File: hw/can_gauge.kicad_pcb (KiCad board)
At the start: 2 copper layers, 31 parts, among them J1 Gauge 1, J2 Gauge 2, J3 Gauge 3, J4 Gauge 4, J5 Gauge 5, J6 Gauge 6, J7 Power & CAN, J8 USB_B, U1 PIC16F1459-IP, U4 74HC595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

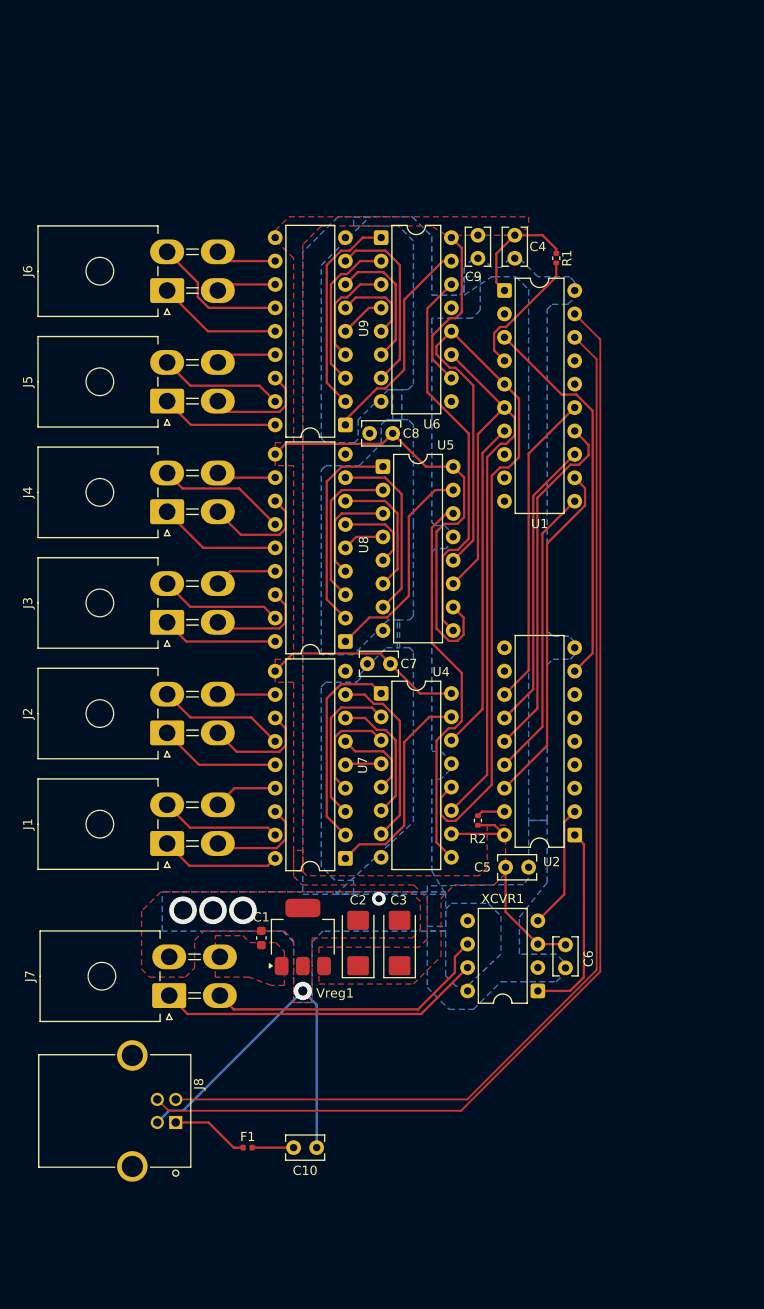
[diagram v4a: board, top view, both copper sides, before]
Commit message: hw: schematic page setup; fix usb wiring
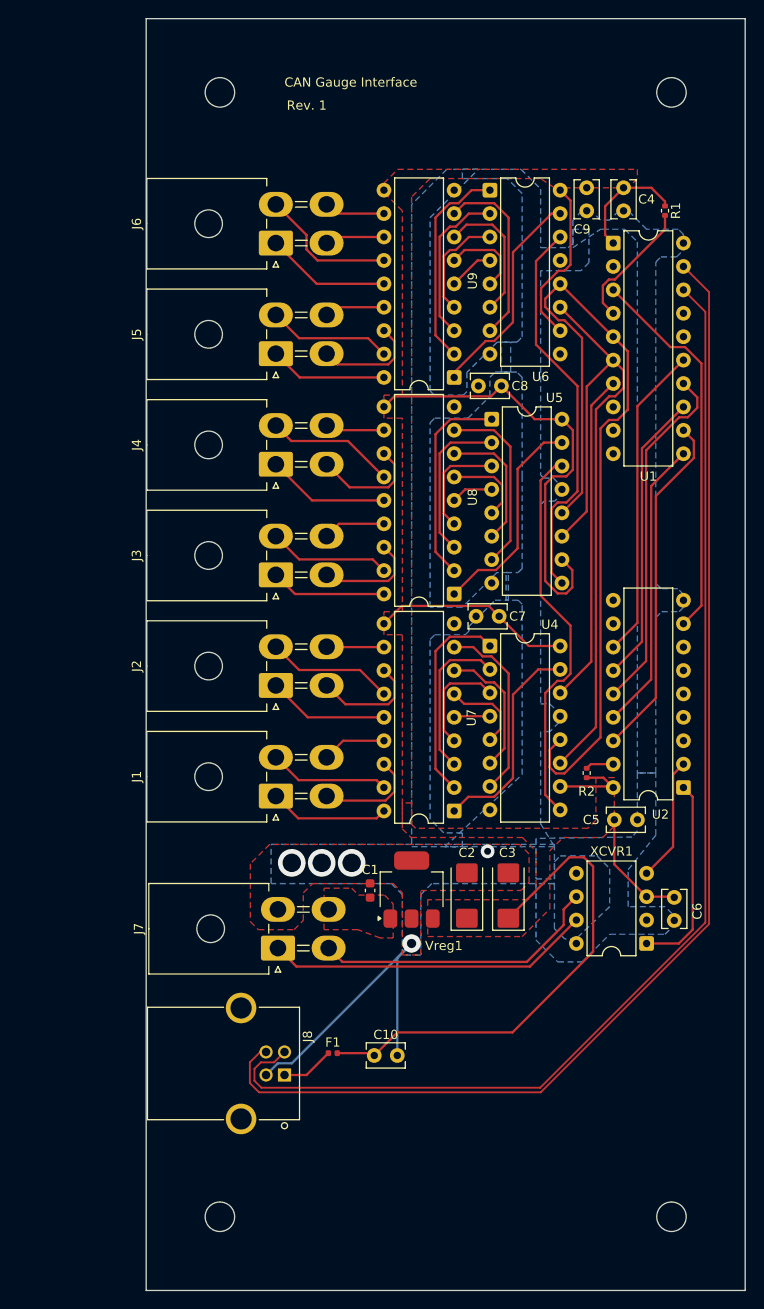
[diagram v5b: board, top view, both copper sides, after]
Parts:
- moved F1 13.8 mm to (70.2, 162.2)
- moved C10 13.3 mm to (77.2, 162.5)
- moved U1 12.9 mm to (100.7, 74.3)
- moved U5 12.9 mm to (87.5, 93.5)
- moved J1 12.9 mm to (64.1, 134.3)
- moved J2 12.9 mm to (64.1, 122.3)
- moved J3 12.9 mm to (64.1, 110.3)
- moved J4 12.9 mm to (64.1, 98.3)
- moved J5 12.9 mm to (64.1, 86.3)
- moved J6 12.9 mm to (64.1, 74.3)
- moved J8 12.9 mm to (65.0, 164.6)
- moved C1 12.9 mm to (74.3, 144.6)
- moved C2 12.9 mm to (84.8, 145.2)
- moved C3 12.9 mm to (89.3, 145.2)
- moved C4 12.9 mm to (101.8, 68.3)
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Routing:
- net +5V: track 128.7 -> 178.4 mm
- net USB-: track 121.1 -> 131.6 mm
- net USB+: track 127.3 -> 134.8 mm
- net GND: track 39.3 -> 34.5 mm
- net Net-(J8-VBUS): track 8.45 -> 5.74 mm
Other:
- board outline added: 65 x 138 mm
- board text added: "CAN Gauge Interface"
- board text added: "Rev. 1"

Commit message: hw: shrink board
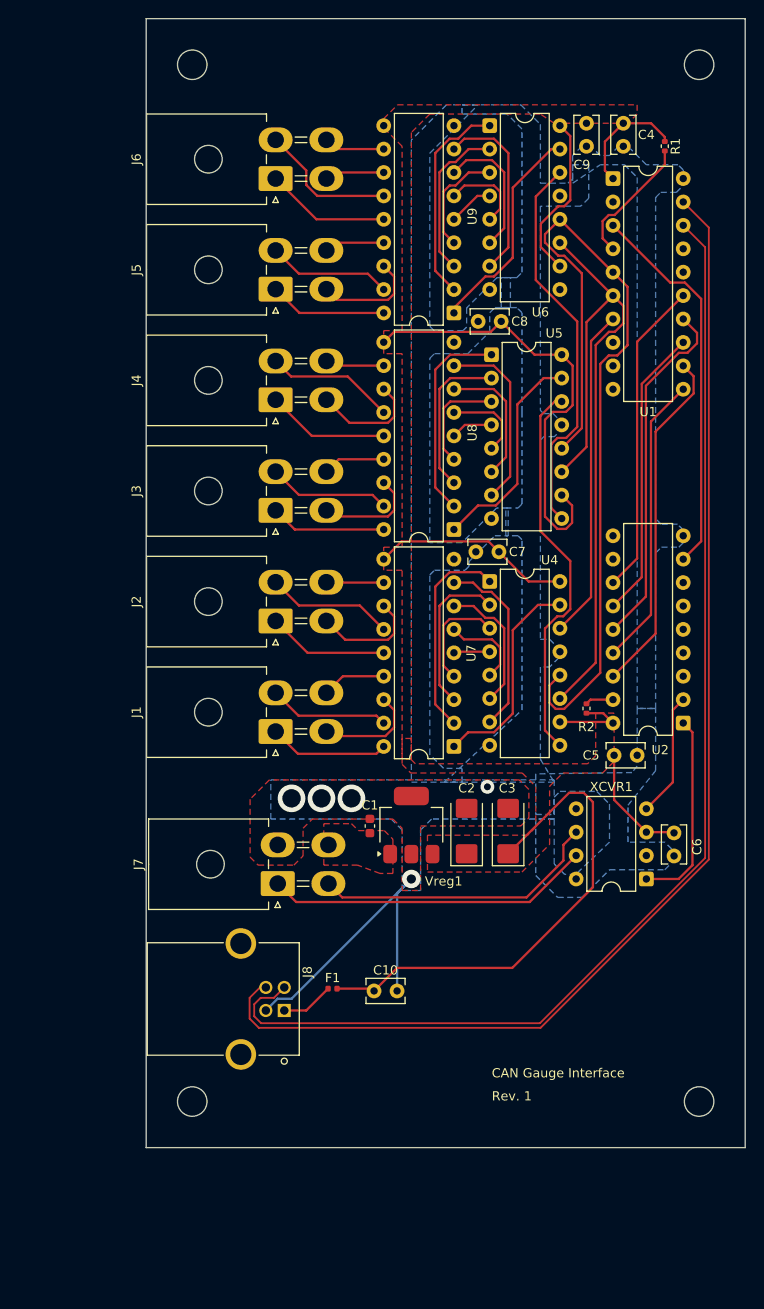
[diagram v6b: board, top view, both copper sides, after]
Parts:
- added REF**: MountingHole_3.2mm_M3, MountingHole:MountingHole_3.2mm_M3, F.Cu at (55.0, 55.0)
- added REF**: MountingHole_3.2mm_M3, MountingHole:MountingHole_3.2mm_M3, F.Cu at (55.0, 167.5)
- added REF**: MountingHole_3.2mm_M3, MountingHole:MountingHole_3.2mm_M3, F.Cu at (110.0, 167.5)
- added REF**: MountingHole_3.2mm_M3, MountingHole:MountingHole_3.2mm_M3, F.Cu at (110.0, 55.0)
- moved C1 7.00 mm to (74.3, 137.6)
- moved C10 7.00 mm to (77.2, 155.5)
- moved C2 7.00 mm to (84.8, 138.2)
- moved C3 7.00 mm to (89.3, 138.2)
- moved C5 7.00 mm to (100.8, 129.9)
- moved C6 7.00 mm to (107.3, 138.3)
- moved C7 7.00 mm to (88.3, 107.8)
- moved C8 7.00 mm to (88.5, 82.8)
- moved F1 7.00 mm to (70.2, 155.2)
- moved J1 7.00 mm to (64.0, 127.3)
- moved J2 7.00 mm to (64.0, 115.3)
- moved J3 7.00 mm to (64.0, 103.3)
- moved J4 7.00 mm to (64.0, 91.3)
- moved J5 7.00 mm to (64.0, 79.3)
- moved J6 7.00 mm to (64.0, 67.3)
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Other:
- board size 65 x 138 mm -> 65 x 122.5 mm

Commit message: hw: fix clipped silkscreen
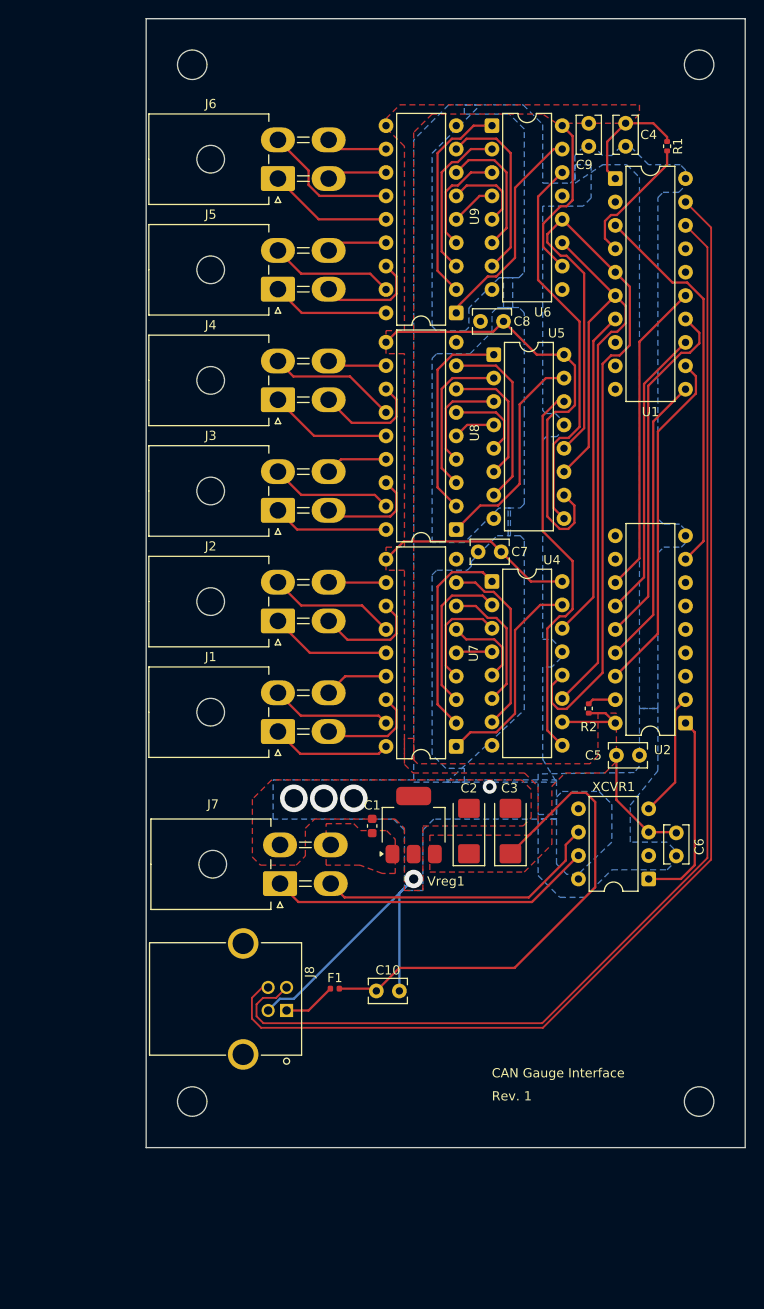
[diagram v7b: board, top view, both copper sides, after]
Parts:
- moved C1 0.25 mm to (74.5, 137.6)
- moved C10 0.25 mm to (77.5, 155.5)
- moved C2 0.25 mm to (85.0, 138.2)
- moved C3 0.25 mm to (89.5, 138.2)
- moved C4 0.25 mm to (102.0, 61.4)
- moved C5 0.25 mm to (101.0, 129.9)
- moved C6 0.25 mm to (107.5, 138.3)
- moved C7 0.25 mm to (88.5, 107.8)
- moved C8 0.25 mm to (88.8, 82.8)
- moved C9 0.25 mm to (98.0, 61.4)
- moved F1 0.25 mm to (70.5, 155.2)
- moved J1 0.25 mm to (64.3, 127.3)
- moved J2 0.25 mm to (64.3, 115.3)
- moved J3 0.25 mm to (64.3, 103.3)
- moved J4 0.25 mm to (64.3, 91.3)
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
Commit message: hw: generate bom and cpl
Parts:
- C1: value 0.47 uF -> 0.47u
- C10, C4, C5, C6, C7, C8, C9: value 0.1 uF -> 0.1u
- C2, C3: value 22 uF -> 22u
- F1: value 500 mA -> 500m
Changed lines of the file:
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@@
 			)
 		)
-		(property "Value" "0.1 uF"
+		(property "Value" "0.1u"
 			(at 1.25 2.5 90)
 			(layer "F.Fab")
@@
 			)
 		)
-		(property "Value" "500 mA"
+		(property "Value" "500m"
 			(at 0 1.17 0)
 			(layer "F.Fab")
@@
 			)
 		)
-		(property "Value" "0.1 uF"
+		(property "Value" "0.1u"
 			(at 1.25 2.5 0)
 			(layer "F.Fab")
@@
 			)
 		)
-		(property "Value" "0.47 uF"
+		(property "Value" "0.47u"
 			(at 0 1.43 90)
 			(layer "F.Fab")
@@
 			)
 		)
-		(property "Value" "0.1 uF"
+		(property "Value" "0.1u"
 			(at 1.25 2.5 0)
 			(layer "F.Fab")
@@
 			)
 		)
-		(property "Value" "0.1 uF"
+		(property "Value" "0.1u"
 			(at 1.25 2.5 0)
 			(layer "F.Fab")
@@
 			)
 		)
-		(property "Value" "22 uF"
+		(property "Value" "22u"
 			(at 0 2.55 90)
 			(layer "F.Fab")
@@
 			)
 		)
-		(property "Value" "0.1 uF"
+		(property "Value" "0.1u"
 			(at 1.25 2.5 90)
 			(layer "F.Fab")
@@
 			)
 		)
-		(property "Value" "22 uF"
+		(property "Value" "22u"
 			(at 0 2.55 90)
 			(layer "F.Fab")
@@
 			)
 		)
-		(property "Value" "0.1 uF"
+		(property "Value" "0.1u"
 			(at 1.25 2.5 270)
 			(layer "F.Fab")
@@
 			)
 		)
-		(property "Value" "0.1 uF"
+		(property "Value" "0.1u"
 			(at 1.25 2.5 0)
 			(layer "F.Fab")
